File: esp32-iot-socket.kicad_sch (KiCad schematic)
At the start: 1 part, among them U1 ESP32-D0WD-V3

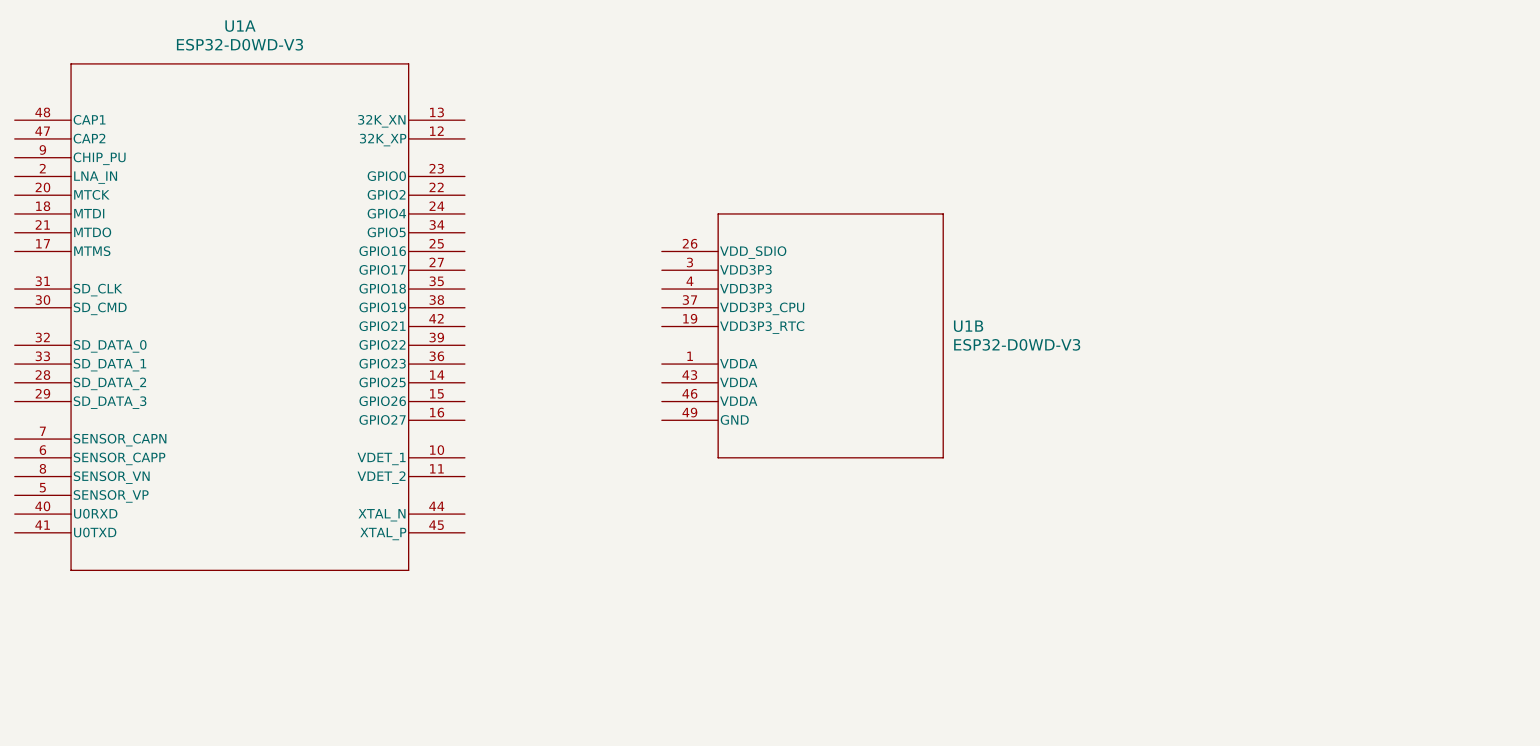
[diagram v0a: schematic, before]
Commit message: proper esp32 footprint added
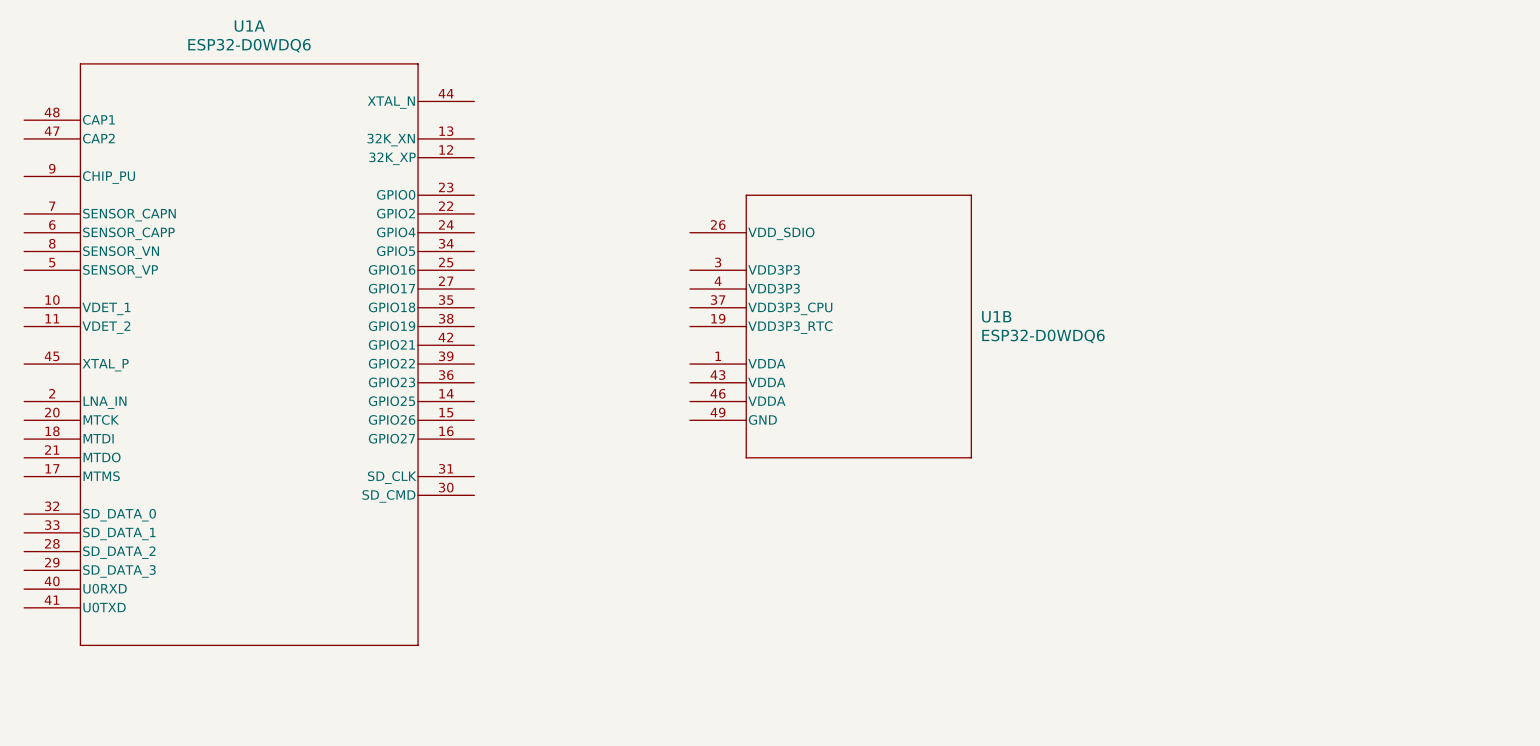
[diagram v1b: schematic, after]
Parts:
- removed U1: ESP32-D0WD-V3, QFN48_ESP32-D0WD-V3_EXP, symbol 2023-07-31_12-32-04:ESP32-D0WD-V3
- added U1: ESP32-D0WDQ6, Package_DFN_QFN:QFN-48-1EP_6x6mm_P0.4mm_EP4.3x4.3mm_ThermalVias, symbol 2023-07-31_14-21-16:ESP32-D0WDQ6
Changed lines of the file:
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@@
 (kicad_sch (version 20230121) (generator eeschema)
   (paper "A4")
-  (symbol (lib_id "2023-07-31_12-32-04:ESP32-D0WD-V3") (at 153.67 88.9 0) (unit 2)
+  (symbol (lib_id "2023-07-31_14-21-16:ESP32-D0WDQ6") (at 157.48 86.36 0) (unit 2)
     (in_bom yes) (on_board yes) (dnp no) (fields_autoplaced)
-    (property "Reference" "U1" (at 193.04 99.06 0)
+    (property "Reference" "U1" (at 196.85 97.79 0)
       (effects (font (size 1.524 1.524)) (justify left))
     )
-    (property "Value" "ESP32-D0WD-V3" (at 193.04 101.6 0)
+    (property "Value" "ESP32-D0WDQ6" (at 196.85 100.33 0)
       (effects (font (size 1.524 1.524)) (justify left))
     )
-    (property "Footprint" "QFN48_ESP32-D0WD-V3_EXP" (at 153.67 88.9 0)
+    (property "Footprint" "Package_DFN_QFN:QFN-48-1EP_6x6mm_P0.4mm_EP4.3x4.3mm_ThermalVias" (at 157.48 86.36 0)
       (effects (font (size 1.27 1.27) italic) hide)
     )
-    (property "Datasheet" "ESP32-D0WD-V3" (at 153.67 88.9 0)
+    (property "Datasheet" "ESP32-D0WDQ6" (at 157.48 86.36 0)
       (effects (font (size 1.27 1.27) italic) hide)
     )
@@
     )
   )
-  (symbol (lib_id "2023-07-31_12-32-04:ESP32-D0WD-V3") (at 66.04 71.12 0) (unit 1)
+  (symbol (lib_id "2023-07-31_14-21-16:ESP32-D0WDQ6") (at 67.31 71.12 0) (unit 1)
     (in_bom yes) (on_board yes) (dnp no) (fields_autoplaced)
-    (property "Reference" "U1" (at 96.52 58.42 0)
+    (property "Reference" "U1" (at 97.79 58.42 0)
       (effects (font (size 1.524 1.524)))
     )
-    (property "Value" "ESP32-D0WD-V3" (at 96.52 60.96 0)
+    (property "Value" "ESP32-D0WDQ6" (at 97.79 60.96 0)
       (effects (font (size 1.524 1.524)))
     )
-    (property "Footprint" "QFN48_ESP32-D0WD-V3_EXP" (at 66.04 71.12 0)
+    (property "Footprint" "Package_DFN_QFN:QFN-48-1EP_6x6mm_P0.4mm_EP4.3x4.3mm_ThermalVias" (at 67.31 71.12 0)
       (effects (font (size 1.27 1.27) italic) hide)
     )
-    (property "Datasheet" "ESP32-D0WD-V3" (at 66.04 71.12 0)
+    (property "Datasheet" "ESP32-D0WDQ6" (at 67.31 71.12 0)
       (effects (font (size 1.27 1.27) italic) hide)
     )

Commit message: hierarchical sheets
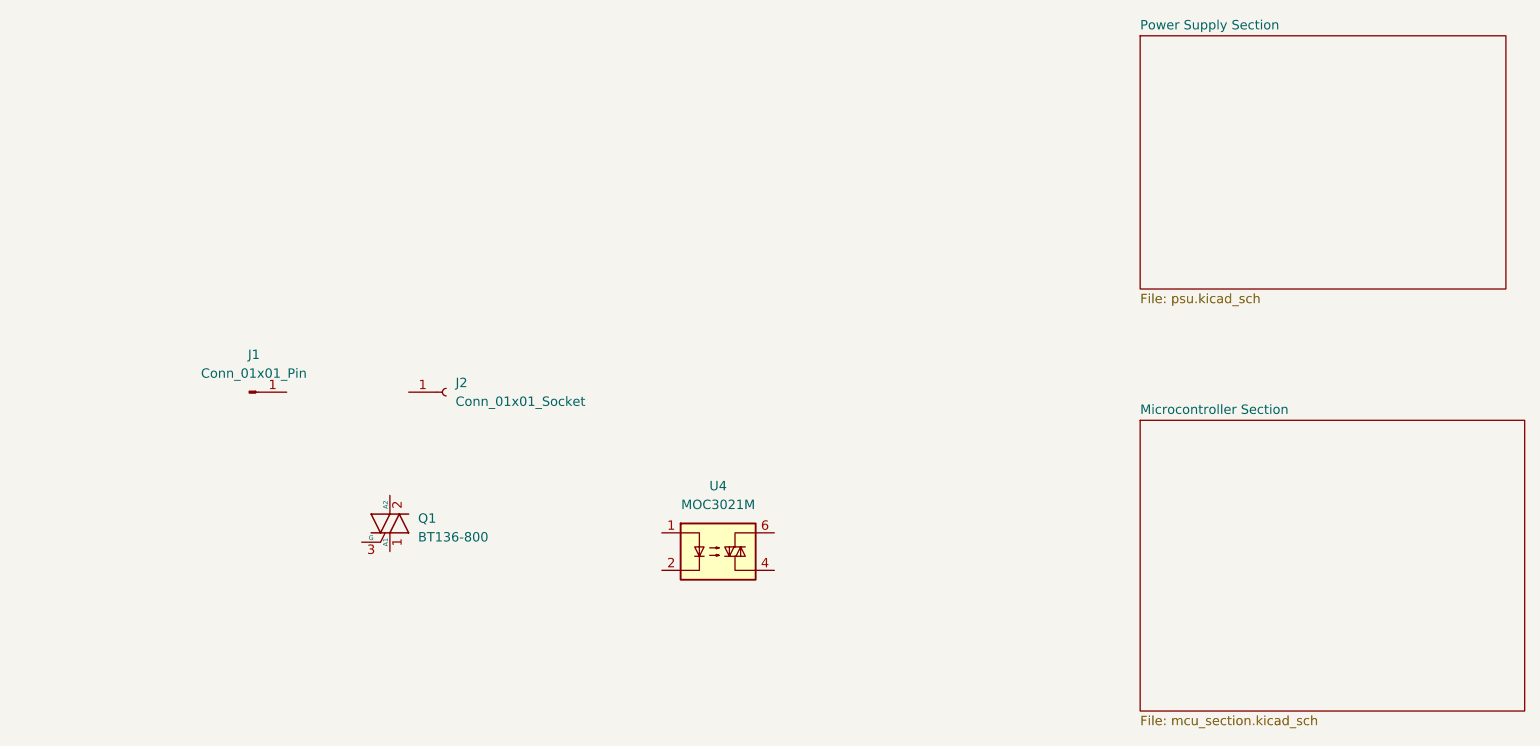
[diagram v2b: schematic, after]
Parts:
- removed U1: ESP32-D0WDQ6, Package_DFN_QFN:QFN-48-1EP_6x6mm_P0.4mm_EP4.3x4.3mm_ThermalVias, symbol 2023-07-31_14-21-16:ESP32-D0WDQ6
- added J1: Conn_01x01_Pin, symbol Connector:Conn_01x01_Pin
- added J2: Conn_01x01_Socket, symbol Connector:Conn_01x01_Socket
- added Q1: BT136-800, Package_TO_SOT_THT:TO-220-3_Vertical, symbol Triac_Thyristor:BT136-800
- added U4: MOC3021M, symbol Relay_SolidState:MOC3021M
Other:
- added sheet Microcontroller Section (mcu_section.kicad_sch)
- added sheet Power Supply Section (psu.kicad_sch)
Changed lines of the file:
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@@
 (kicad_sch (version 20230121) (generator eeschema)
   (paper "A4")
-  (symbol (lib_id "2023-07-31_14-21-16:ESP32-D0WDQ6") (at 157.48 86.36 0) (unit 2)
+  (symbol (lib_id "Relay_SolidState:MOC3021M") (at 161.29 129.54 0) (unit 1)
     (in_bom yes) (on_board yes) (dnp no) (fields_autoplaced)
-    (property "Reference" "U1" (at 196.85 97.79 0)
-      (effects (font (size 1.524 1.524)) (justify left))
+    (property "Reference" "U4" (at 161.29 120.65 0)
+      (effects (font (size 1.27 1.27)))
     )
-    (property "Value" "ESP32-D0WDQ6" (at 196.85 100.33 0)
-      (effects (font (size 1.524 1.524)) (justify left))
+    (property "Value" "MOC3021M" (at 161.29 123.19 0)
+      (effects (font (size 1.27 1.27)))
     )
-    (property "Footprint" "Package_DFN_QFN:QFN-48-1EP_6x6mm_P0.4mm_EP4.3x4.3mm_ThermalVias" (at 157.48 86.36 0)
-      (effects (font (size 1.27 1.27) italic) hide)
+    (property "Footprint" "" (at 156.21 134.62 0)
+      (effects (font (size 1.27 1.27) italic) (justify left) hide)
     )
-    (property "Datasheet" "ESP32-D0WDQ6" (at 157.48 86.36 0)
-      (effects (font (size 1.27 1.27) italic) hide)
+    (property "Datasheet" "https://www.onsemi.com/pub/Collateral/MOC3023M-D.PDF" (at 161.29 129.54 0)
+      (effects (font (size 1.27 1.27)) (justify left) hide)
     )
-    (pin "10")
-    (pin "11")
-    (pin "12")
-    (pin "13")
-    (pin "14")
-    (pin "15")
-    (pin "16")
-    (pin "17")
-    (pin "18")
+    (pin "1")
     (pin "2")
-    (pin "20")
-    (pin "21")
-    (pin "22")
-    (pin "23")
-    (pin "24")
-    (pin "25")
-    (pin "27")
-    (pin "28")
-    (pin "29")
-    (pin "30")
-    (pin "31")
-    (pin "32")
-    (pin "33")
-    (pin "34")
-    (pin "35")
-    (pin "36")
-    (pin "38")
-    (pin "39")
-    (pin "40")
-    (pin "41")
-    (pin "42")
-    (pin "44")
-    (pin "45")
-    (pin "47")
-    (pin "48")
+    (pin "3")
+    (pin "4")
     (pin "5")
     (pin "6")
-    (pin "7")
-    (pin "8")
-    (pin "9")
-    (pin "1")
-    (pin "19")
-    (pin "26")
-    (pin "3")
-    (pin "37")
-    (pin "4")
-    (pin "43")
-    (pin "46")
-    (pin "49")
     (instances
       (project "esp32-iot-socket"
         (path "/45e1e5e5-a388-432c-8d2b-80b7f8345075"
-          (reference "U1") (unit 2)
+          (reference "U4") (unit 1)
         )
       )
     )
   )
-  (symbol (lib_id "2023-07-31_14-21-16:ESP32-D0WDQ6") (at 67.31 71.12 0) (unit 1)
+  (symbol (lib_id "Connector:Conn_01x01_Socket") (at 124.46 107.95 0) (unit 1)
     (in_bom yes) (on_board yes) (dnp no) (fields_autoplaced)
-    (property "Reference" "U1" (at 97.79 58.42 0)
-      (effects (font (size 1.524 1.524)))
+    (property "Reference" "J2" (at 125.73 106.68 0)
+      (effects (font (size 1.27 1.27)) (justify left))
     )
-    (property "Value" "ESP32-D0WDQ6" (at 97.79 60.96 0)
-      (effects (font (size 1.524 1.524)))
+    (property "Value" "Conn_01x01_Socket" (at 125.73 109.22 0)
+      (effects (font (size 1.27 1.27)) (justify left))
     )
-    (property "Footprint" "Package_DFN_QFN:QFN-48-1EP_6x6mm_P0.4mm_EP4.3x4.3mm_ThermalVias" (at 67.31 71.12 0)
-      (effects (font (size 1.27 1.27) italic) hide)
+    (property "Footprint" "" (at 124.46 107.95 0)
+      (effects (font (size 1.27 1.27)) hide)
     )
-    (property "Datasheet" "ESP32-D0WDQ6" (at 67.31 71.12 0)
-      (effects (font (size 1.27 1.27) italic) hide)
+    (property "Datasheet" "~" (at 124.46 107.95 0)
+      (effects (font (size 1.27 1.27)) hide)
     )
-    (pin "10")
-    (pin "11")
-    (pin "12")
-    (pin "13")
-    (pin "14")
-    (pin "15")
-    (pin "16")
-    (pin "17")
-    (pin "18")
-    (pin "2")
-    (pin "20")
-    (pin "21")
-    (pin "22")
-    (pin "23")
-    (pin "24")
-    (pin "25")
-    (pin "27")
-    (pin "28")
-    (pin "29")
-    (pin "30")
-    (pin "31")
-    (pin "32")
-    (pin "33")
-    (pin "34")
-    (pin "35")
-    (pin "36")
-    (pin "38")
-    (pin "39")
-    (pin "40")
-    (pin "41")
-    (pin "42")
-    (pin "44")
-    (pin "45")
-    (pin "47")
-    (pin "48")
-    (pin "5")
-    (pin "6")
-    (pin "7")
-    (pin "8")
-    (pin "9")
     (pin "1")
-    (pin "19")
-    (pin "26")
-    (pin "3")
-    (pin "37")
-    (pin "4")
-    (pin "43")
-    (pin "46")
-    (pin "49")
     (instances
       (project "esp32-iot-socket"
         (path "/45e1e5e5-a388-432c-8d2b-80b7f8345075"
-          (reference "U1") (unit 1)
+          (reference "J2") (unit 1)
         )
       )
     )
+  )
+  (symbol (lib_id "Triac_Thyristor:BT136-800") (at 116.84 125.73 0) (unit 1)
+    (in_bom yes) (on_board yes) (dnp no) (fields_autoplaced)
+    (property "Reference" "Q1" (at 120.65 125.0442 0)
+      (effects (font (size 1.27 1.27)) (justify left))
+    )
+    (property "Value" "BT136-800" (at 120.65 127.5842 0)
+      (effects (font (size 1.27 1.27)) (justify left))
+    )
+    (property "Footprint" "Package_TO_SOT_THT:TO-220-3_Vertical" (at 121.92 127.635 0)
+      (effects (font (size 1.27 1.27) italic) (justify left) hide)
+    )
+    (property "Datasheet" "http://www.micropik.com/PDF/BT136-600.pdf" (at 116.84 125.73 0)
+      (effects (font (size 1.27 1.27)) (justify left) hide)
+    )
+    (pin "1")
+    (pin "2")
+    (pin "3")
+    (instances
+      (project "esp32-iot-socket"
+        (path "/45e1e5e5-a388-432c-8d2b-80b7f8345075"
+          (reference "Q1") (unit 1)
+        )
+      )
+    )
+  )
+  (symbol (lib_id "Connector:Conn_01x01_Pin") (at 97.79 107.95 0) (unit 1)
+    (in_bom yes) (on_board yes) (dnp no) (fields_autoplaced)
+    (property "Reference" "J1" (at 98.425 102.87 0)
+      (effects (font (size 1.27 1.27)))
+    )
+    (property "Value" "Conn_01x01_Pin" (at 98.425 105.41 0)
+      (effects (font (size 1.27 1.27)))
+    )
+    (property "Footprint" "" (at 97.79 107.95 0)
+      (effects (font (size 1.27 1.27)) hide)
+    )
+    (property "Datasheet" "~" (at 97.79 107.95 0)
+      (effects (font (size 1.27 1.27)) hide)
+    )
+    (pin "1")
+    (instances
+      (project "esp32-iot-socket"
+        (path "/45e1e5e5-a388-432c-8d2b-80b7f8345075"
+          (reference "J1") (unit 1)
+        )
+      )
+    )
+  )
+  (sheet (at 218.44 111.76) (size 52.07 39.37) (fields_autoplaced)
+    (stroke (width 0.1524) (type solid))
+    (fill (color 0 0 0 0.0000))
+    (property "Sheetname" "Microcontroller Section" (at 218.44 111.0484 0)
+      (effects (font (size 1.27 1.27)) (justify left bottom))
+    )
+    (property "Sheetfile" "mcu_section.kicad_sch" (at 218.44 151.7146 0)
+      (effects (font (size 1.27 1.27)) (justify left top))
+    )
+    (instances
+      (project "esp32-iot-socket"
+        (path "/45e1e5e5-a388-432c-8d2b-80b7f8345075" (page "3"))
+      )
+    )
+  )
+  (sheet (at 218.44 59.69) (size 49.53 34.29) (fields_autoplaced)
+    (stroke (width 0.1524) (type solid))
+    (fill (color 0 0 0 0.0000))
+    (property "Sheetname" "Power Supply Section" (at 218.44 58.9784 0)
+      (effects (font (size 1.27 1.27)) (justify left bottom))
+    )
+    (property "Sheetfile" "psu.kicad_sch" (at 218.44 94.5646 0)
+      (effects (font (size 1.27 1.27)) (justify left top))
+    )
+    (instances
+      (project "esp32-iot-socket"
+        (path "/45e1e5e5-a388-432c-8d2b-80b7f8345075" (page "2"))
+      )
+    )

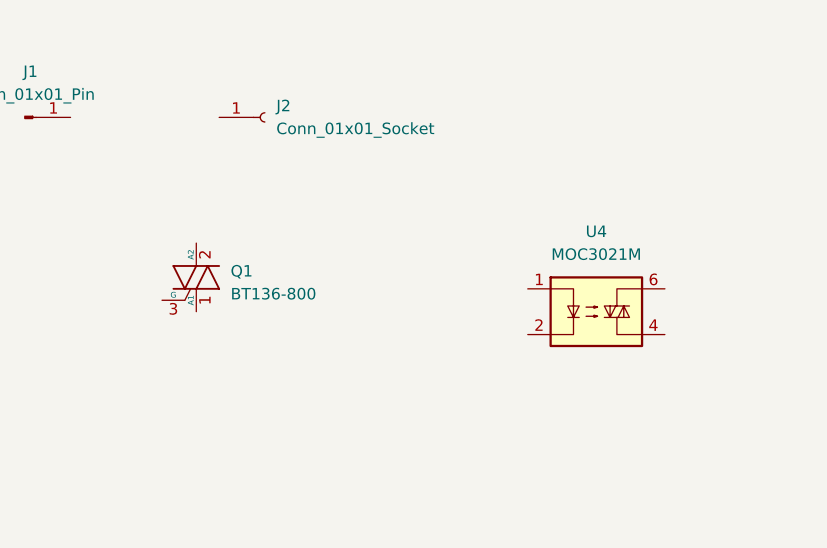
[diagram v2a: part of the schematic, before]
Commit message: progress in psu section:footprints added:flyback ic yet to be added
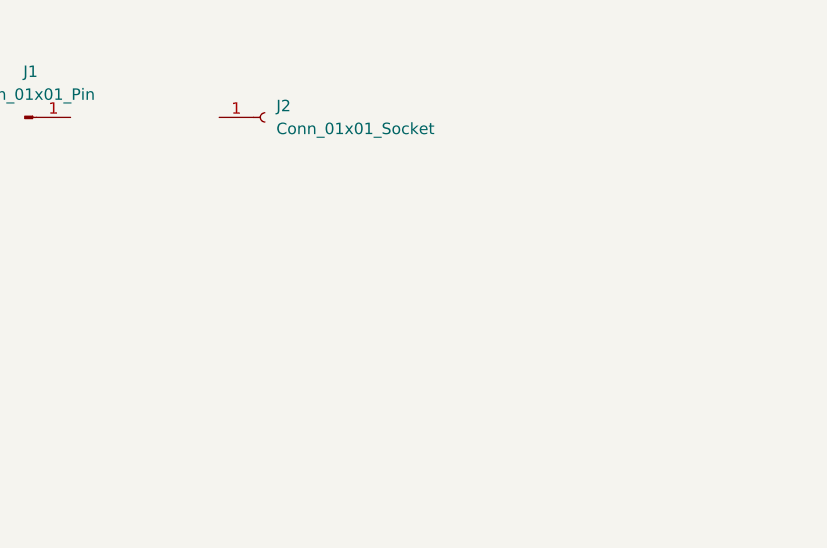
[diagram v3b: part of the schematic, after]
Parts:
- removed Q1: BT136-800, Package_TO_SOT_THT:TO-220-3_Vertical, symbol Triac_Thyristor:BT136-800
- removed U4: MOC3021M, symbol Relay_SolidState:MOC3021M
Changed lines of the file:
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@@
 (kicad_sch (version 20230121) (generator eeschema)
   (paper "A4")
-  (symbol (lib_id "Relay_SolidState:MOC3021M") (at 161.29 129.54 0) (unit 1)
-    (in_bom yes) (on_board yes) (dnp no) (fields_autoplaced)
-    (property "Reference" "U4" (at 161.29 120.65 0)
-      (effects (font (size 1.27 1.27)))
-    )
-    (property "Value" "MOC3021M" (at 161.29 123.19 0)
-      (effects (font (size 1.27 1.27)))
-    )
-    (property "Footprint" "" (at 156.21 134.62 0)
-      (effects (font (size 1.27 1.27) italic) (justify left) hide)
-    )
-    (property "Datasheet" "https://www.onsemi.com/pub/Collateral/MOC3023M-D.PDF" (at 161.29 129.54 0)
-      (effects (font (size 1.27 1.27)) (justify left) hide)
-    )
-    (pin "1")
-    (pin "2")
-    (pin "3")
-    (pin "4")
-    (pin "5")
-    (pin "6")
-    (instances
-      (project "esp32-iot-socket"
-        (path "/45e1e5e5-a388-432c-8d2b-80b7f8345075"
-          (reference "U4") (unit 1)
-        )
-      )
-    )
-  )
   (symbol (lib_id "Connector:Conn_01x01_Socket") (at 124.46 107.95 0) (unit 1)
     (in_bom yes) (on_board yes) (dnp no) (fields_autoplaced)
@@
         )
       )
-    )
-  )
-  (symbol (lib_id "Triac_Thyristor:BT136-800") (at 116.84 125.73 0) (unit 1)
-    (in_bom yes) (on_board yes) (dnp no) (fields_autoplaced)
-    (property "Reference" "Q1" (at 120.65 125.0442 0)
-      (effects (font (size 1.27 1.27)) (justify left))
-    )
-    (property "Value" "BT136-800" (at 120.65 127.5842 0)
-      (effects (font (size 1.27 1.27)) (justify left))
-    )
-    (property "Footprint" "Package_TO_SOT_THT:TO-220-3_Vertical" (at 121.92 127.635 0)
-      (effects (font (size 1.27 1.27) italic) (justify left) hide)
-    )
-    (property "Datasheet" "http://www.micropik.com/PDF/BT136-600.pdf" (at 116.84 125.73 0)
-      (effects (font (size 1.27 1.27)) (justify left) hide)
-    )
-    (pin "1")
-    (pin "2")
-    (pin "3")
-    (instances
-      (project "esp32-iot-socket"
-        (path "/45e1e5e5-a388-432c-8d2b-80b7f8345075"
-          (reference "Q1") (unit 1)
-        )
-      )
